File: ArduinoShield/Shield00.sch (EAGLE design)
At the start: 105 parts, among them T1 BC337, T10 BC337, T11 BC337, T12 BC337, T13 BC337, T14 BC337, T15 BC337, T16 BC337, T2 BC337, T3 BC337, T4 BC337, T5 BC337, T6 BC337, T7 BC337, T8 BC337, T9 BC337

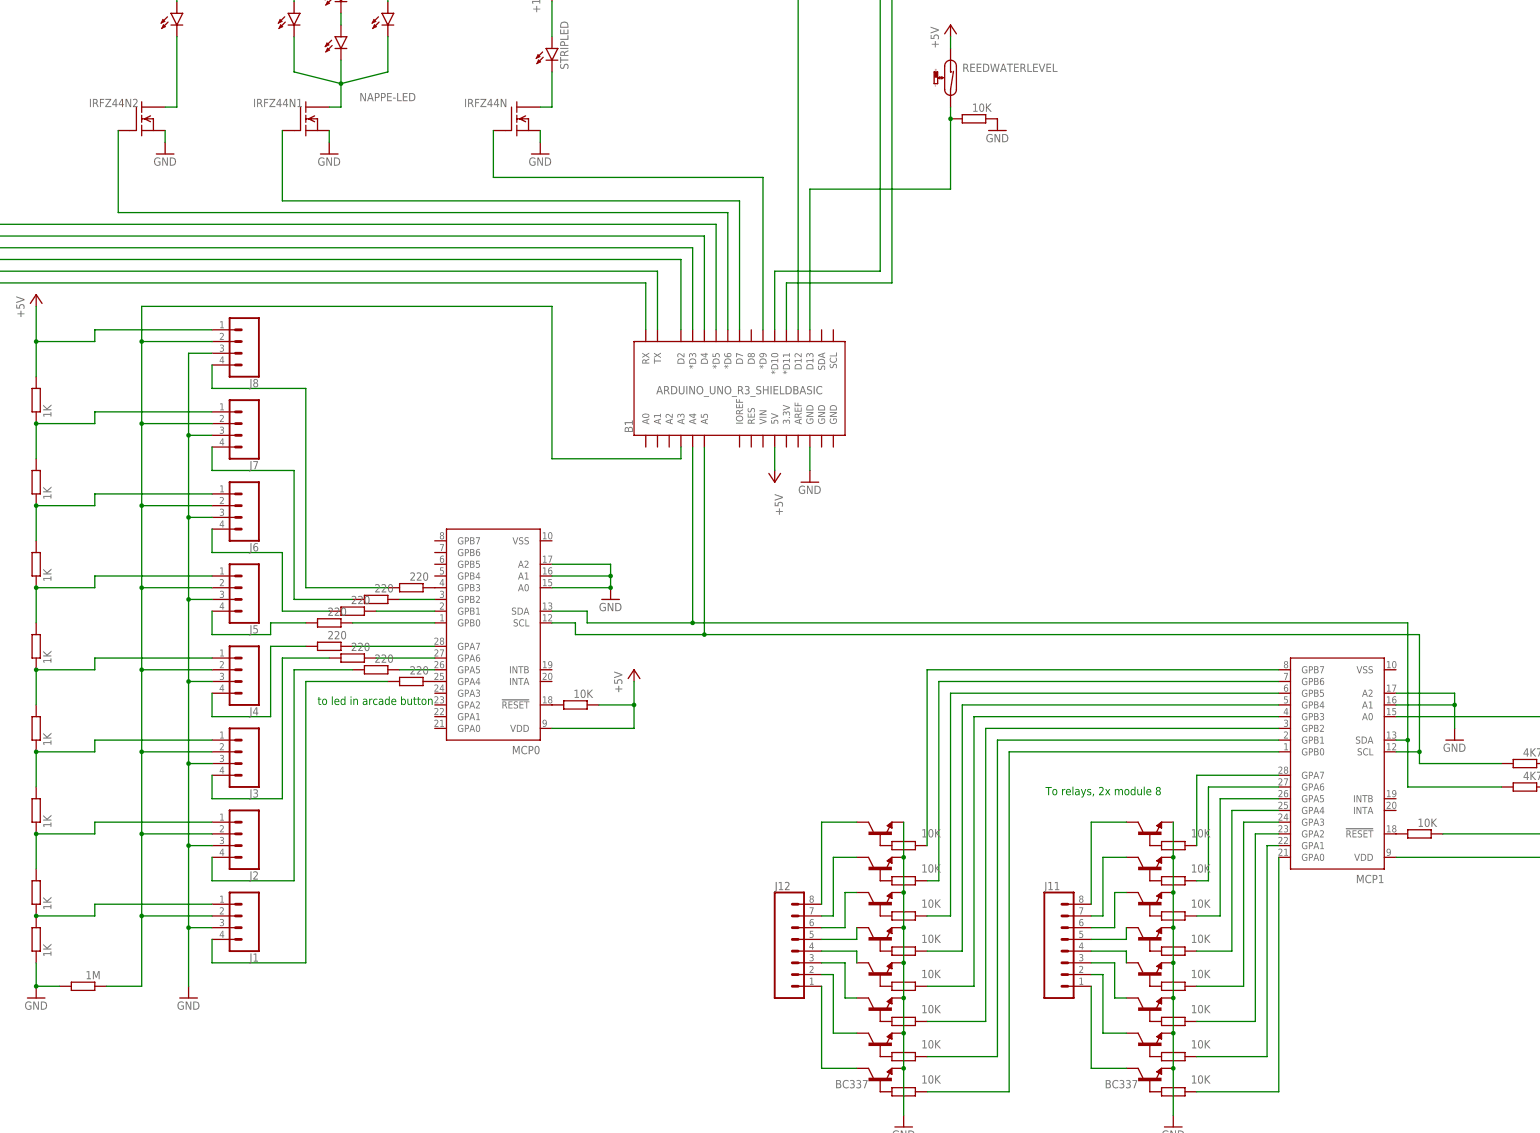
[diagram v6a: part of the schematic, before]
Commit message: change to 2N4401 and connection to VSS
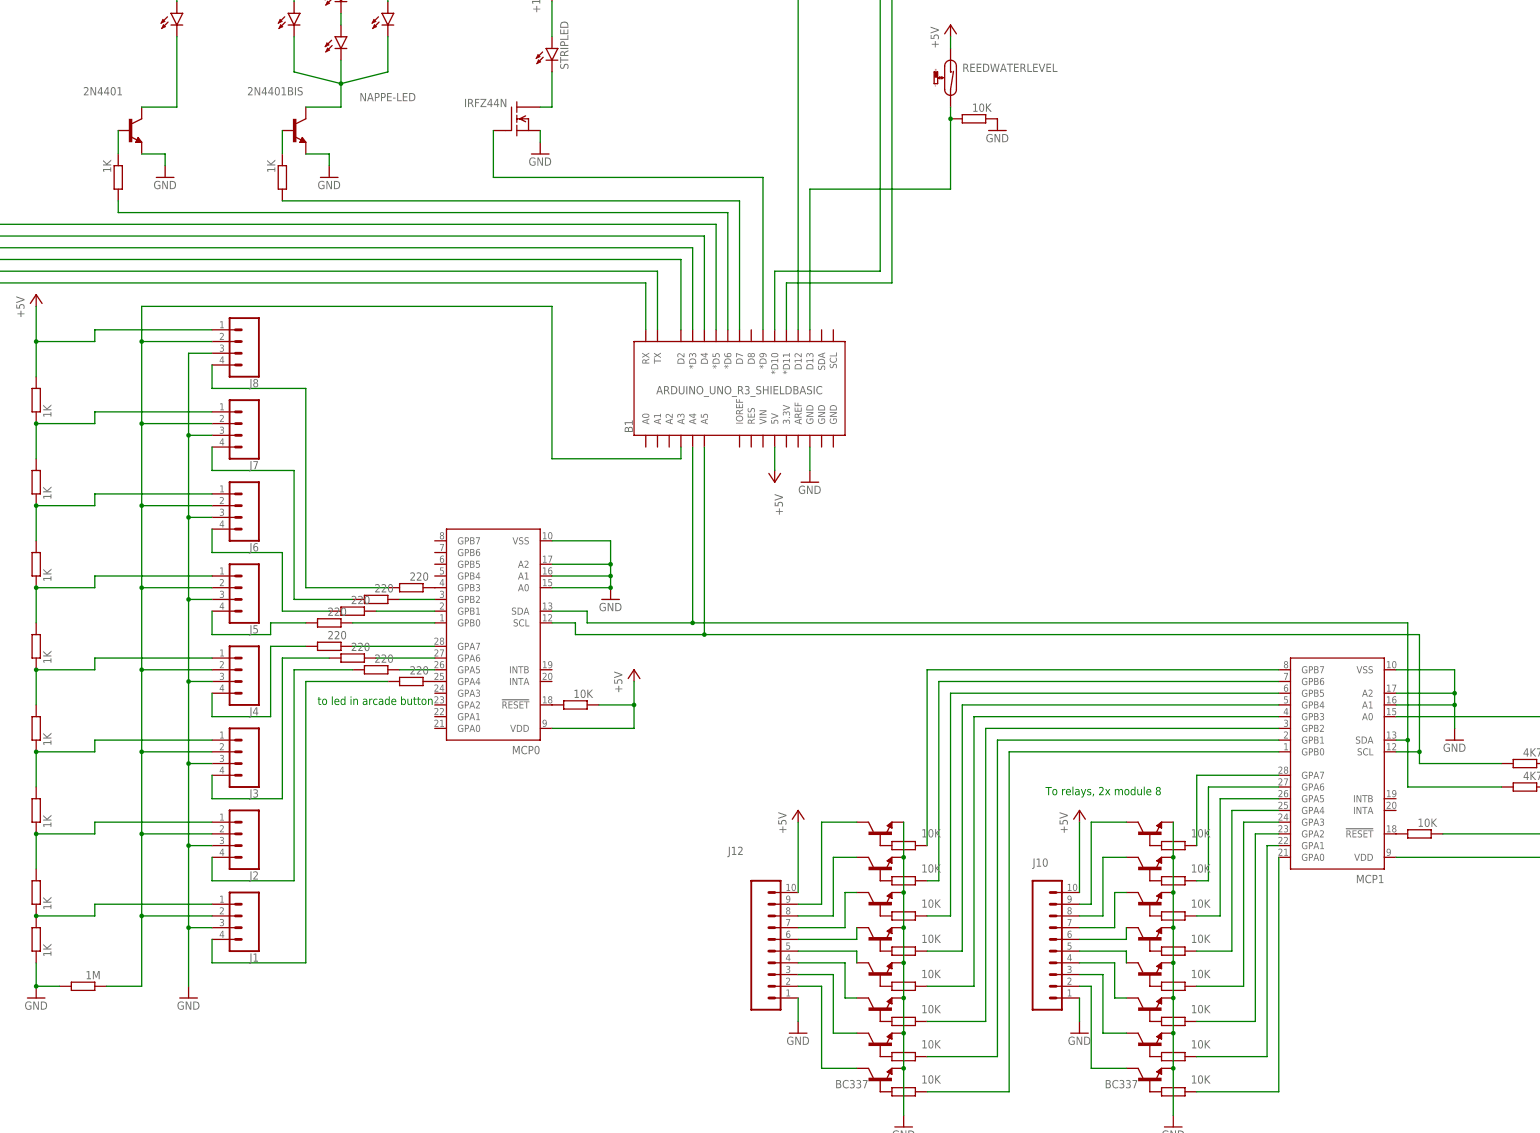
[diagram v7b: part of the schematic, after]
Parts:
- removed IRFZ44N1, IRFZ44N2: IRF840, transistor-fet:IRF840
- removed J11: (no value), SparkFun-Connectors:CONN_08"
- added 2N4401, 2N4401BIS: 2N4416, transistor-neu-to92:2N4416
- added J10: (no value), SparkFun-Connectors:CONN_10"
- added R26, R43: 1K, rcl:R-EU_R0805
- J12: device SparkFun-Connectors:CONN_08" -> SparkFun-Connectors:CONN_10"
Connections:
- new net N$87: 2N4401.B, R26.1
- new net N$88: 2N4401BIS.B, R43.1
- net +5V: now also J10.10, J12.10
- net GND: now also 2N4401.E, 2N4401BIS.E, J10.1, J12.1, MCP0.VSS, MCP1.VSS; no longer IRFZ44N1.S, IRFZ44N2.S
- net N$101: now also R43.2; no longer IRFZ44N1.G
- net N$115: now also 2N4401.C; no longer IRFZ44N2.D
- net N$116: now also R26.2; no longer IRFZ44N2.G
- net N$70: now also J10.5; no longer J11.4
- net N$71: now also J10.6; no longer J11.5
- net N$72: now also J10.7; no longer J11.6
- net N$73: now also J10.8; no longer J11.7
- net N$74: now also J10.9; no longer J11.8
- net N$75: now also J10.4; no longer J11.3
- net N$76: now also J10.3; no longer J11.2
- net N$77: now also J10.2; no longer J11.1
- net N$78: now also J12.6, T13.C; no longer J12.4, T12.C
- net N$79: now also T12.C; no longer T13.C
- net N$80: now also J12.4, T11.C; no longer J12.6, T14.C
- net N$81: now also T14.C; no longer T15.C
- net N$82: now also J12.3, T10.C; no longer J12.8, T16.C
- net N$83: now also J12.2, T9.C; no longer J12.3, T11.C
- net N$84: now also J12.8, T15.C; no longer J12.2, T10.C
- net N$85: now also J12.9, T16.C; no longer J12.1, T9.C
- net N$99: now also 2N4401BIS.C; no longer IRFZ44N1.D

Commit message: correction suite à la remise
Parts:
- added C1, C2: 100uF, capacitor-wima:C5/3
- added S1: MOMENTARY-SWITCH-SPST-PTH-6.0MM, SparkFun-Switches:MOMENTARY-SWITCH-SPST-PTH-6.0MM
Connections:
- new net N$89: B1.RES, S1.1
- net +5V: now also B1.VIN, C1.2, C2.2; no longer B1.5V
- net GND: now also C1.1, C2.1, S1.2
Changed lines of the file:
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@@
 <part name="R26" library="rcl" library_urn="urn:adsk.eagle:library:334" deviceset="R-EU_" device="R0805" package3d_urn="urn:adsk.eagle:package:23553/2" value="1K"/>
 <part name="R43" library="rcl" library_urn="urn:adsk.eagle:library:334" deviceset="R-EU_" device="R0805" package3d_urn="urn:adsk.eagle:package:23553/2" value="1K"/>
+<part name="C1" library="capacitor-wima" library_urn="urn:adsk.eagle:library:116" deviceset="C" device="5/3" package3d_urn="urn:adsk.eagle:package:5433/1" value="100uF"/>
+<part name="C2" library="capacitor-wima" library_urn="urn:adsk.eagle:library:116" deviceset="C" device="5/3" package3d_urn="urn:adsk.eagle:package:5433/1" value="100uF"/>
+<part name="S1" library="SparkFun-Switches" library_urn="urn:adsk.eagle:library:535" deviceset="MOMENTARY-SWITCH-SPST" device="-PTH-6.0MM" package3d_urn="urn:adsk.eagle:package:40163/1"/>
+<part name="GND16" library="supply1" library_urn="urn:adsk.eagle:library:371" deviceset="GND" device=""/>
 </parts>
 <sheets>
@@
 <attribute name="VALUE" x="383.794" y="128.27" size="1.778" layer="96" font="vector" rot="R180" align="top-left"/>
 </instance>
-<instance part="P+3" gate="1" x="373.38" y="109.22" smashed="yes" rot="R180">
-<attribute name="VALUE" x="373.38" y="106.68" size="1.778" layer="96" rot="R270"/>
+<instance part="P+3" gate="1" x="370.84" y="101.6" smashed="yes" rot="R180">
+<attribute name="VALUE" x="370.84" y="99.06" size="1.778" layer="96" rot="R270"/>
 </instance>
 <instance part="GND4" gate="1" x="381" y="109.22" smashed="yes">
@@
 <attribute name="NAME" x="268.1986" y="179.07" size="1.778" layer="95" rot="R270" display="off"/>
 <attribute name="VALUE" x="263.398" y="179.07" size="1.778" layer="96" rot="R270"/>
+</instance>
+<instance part="C1" gate="G$1" x="523.24" y="68.58" smashed="yes" rot="R90">
+<attribute name="NAME" x="522.859" y="70.104" size="1.778" layer="95" rot="R90"/>
+<attribute name="VALUE" x="525.399" y="72.644" size="1.778" layer="96"/>
+</instance>
+<instance part="C2" gate="G$1" x="340.36" y="96.52" smashed="yes" rot="R90">
+<attribute name="NAME" x="339.979" y="98.044" size="1.778" layer="95" rot="R90"/>
+<attribute name="VALUE" x="342.519" y="100.584" size="1.778" layer="96"/>
+</instance>
+<instance part="S1" gate="G$1" x="386.08" y="91.44" smashed="yes">
+<attribute name="NAME" x="386.08" y="92.964" size="1.778" layer="95" font="vector" align="bottom-center"/>
+<attribute name="VALUE" x="386.08" y="90.932" size="1.778" layer="96" font="vector" align="top-center"/>
+</instance>
+<instance part="GND16" gate="1" x="398.78" y="86.36" smashed="yes">
+<attribute name="VALUE" x="396.24" y="83.82" size="1.778" layer="96"/>
 </instance>
 </instances>
@@
 <wire x1="337.82" y1="96.52" x2="337.82" y2="91.44" width="0.1524" layer="91"/>
 <junction x="337.82" y="91.44"/>
+<pinref part="C2" gate="G$1" pin="1"/>
+<junction x="337.82" y="96.52"/>
 </segment>
 <segment>
@@
 <wire x1="520.7" y1="68.58" x2="520.7" y2="63.5" width="0.1524" layer="91"/>
 <junction x="520.7" y="63.5"/>
+<pinref part="C1" gate="G$1" pin="1"/>
+<junction x="520.7" y="68.58"/>
 </segment>
 <segment>
@@
 <wire x1="439.42" y1="-2.54" x2="439.42" y2="-7.62" width="0.1524" layer="91"/>
 </segment>
+<segment>
+<pinref part="S1" gate="G$1" pin="2"/>
+<pinref part="GND16" gate="1" pin="GND"/>
+<wire x1="391.16" y1="91.44" x2="398.78" y2="91.44" width="0.1524" layer="91"/>
+<wire x1="398.78" y1="91.44" x2="398.78" y2="88.9" width="0.1524" layer="91"/>
+</segment>
 </net>
 <net name="N$1" class="0">
@@
 <wire x1="335.28" y1="60.96" x2="342.9" y2="60.96" width="0.1524" layer="91"/>
 <junction x="342.9" y="60.96"/>
-</segment>
-<segment>
-<pinref part="P+3" gate="1" pin="+5V"/>
-<pinref part="B1" gate="G$1" pin="5V"/>
-<wire x1="373.38" y1="111.76" x2="373.38" y2="116.84" width="0.1524" layer="91"/>
+<pinref part="C2" gate="G$1" pin="2"/>
+<wire x1="345.44" y1="96.52" x2="347.98" y2="96.52" width="0.1524" layer="91"/>
+<wire x1="347.98" y1="96.52" x2="347.98" y2="55.88" width="0.1524" layer="91"/>
+<wire x1="347.98" y1="55.88" x2="342.9" y2="55.88" width="0.1524" layer="91"/>
+<junction x="342.9" y="55.88"/>
 </segment>
 <segment>
@@
 <segment>
 <pinref part="MCP1" gate="G$1" pin="VDD"/>
-<wire x1="508" y1="27.94" x2="546.1" y2="27.94" width="0.1524" layer="91"/>
+<wire x1="508" y1="27.94" x2="528.32" y2="27.94" width="0.1524" layer="91"/>
 <pinref part="P+6" gate="1" pin="+5V"/>
+<wire x1="528.32" y1="27.94" x2="546.1" y2="27.94" width="0.1524" layer="91"/>
 <wire x1="546.1" y1="27.94" x2="546.1" y2="33.02" width="0.1524" layer="91"/>
 <pinref part="R22" gate="G$1" pin="1"/>
@@
 <wire x1="541.02" y1="43.18" x2="546.1" y2="43.18" width="0.1524" layer="91"/>
 <junction x="546.1" y="43.18"/>
+<pinref part="C1" gate="G$1" pin="2"/>
+<wire x1="528.32" y1="68.58" x2="528.32" y2="27.94" width="0.1524" layer="91"/>
+<junction x="528.32" y="27.94"/>
 </segment>
 <segment>
@@
 <pinref part="P+9" gate="1" pin="+5V"/>
 <wire x1="439.42" y1="20.32" x2="439.42" y2="35.56" width="0.1524" layer="91"/>
+</segment>
+<segment>
+<pinref part="B1" gate="G$1" pin="VIN"/>
+<pinref part="P+3" gate="1" pin="+5V"/>
+<wire x1="370.84" y1="116.84" x2="370.84" y2="104.14" width="0.1524" layer="91"/>
 </segment>
 </net>
@@
 </segment>
 </net>
+<net name="N$89" class="0">
+<segment>
+<pinref part="B1" gate="G$1" pin="RES"/>
+<wire x1="368.3" y1="116.84" x2="368.3" y2="91.44" width="0.1524" layer="91"/>
+<pinref part="S1" gate="G$1" pin="1"/>
+<wire x1="368.3" y1="91.44" x2="381" y2="91.44" width="0.1524" layer="91"/>
+</segment>
+</net>
